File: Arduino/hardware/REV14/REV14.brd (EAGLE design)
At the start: 50 x 50 mm, 23 parts, among them IC2 ATMEGA168-AU, Q1 32768Hz, U1 RN2483, U4 SHT21, X1 SMA-142-0701-881/886, X2 SMA-142-0701-881/886

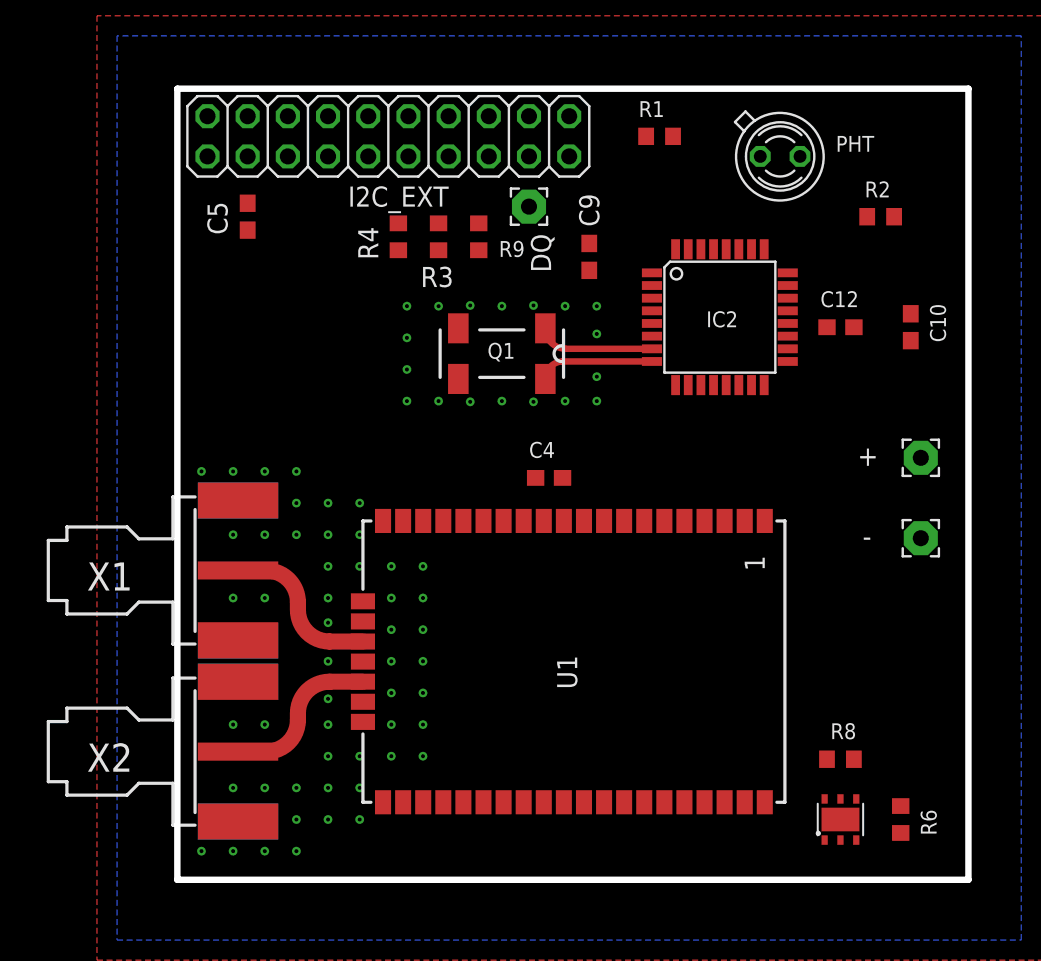
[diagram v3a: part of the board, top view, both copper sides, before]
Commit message: updated readme...
2-4 set of docs are confusing.... it makes things far more dificult for
those that do the work
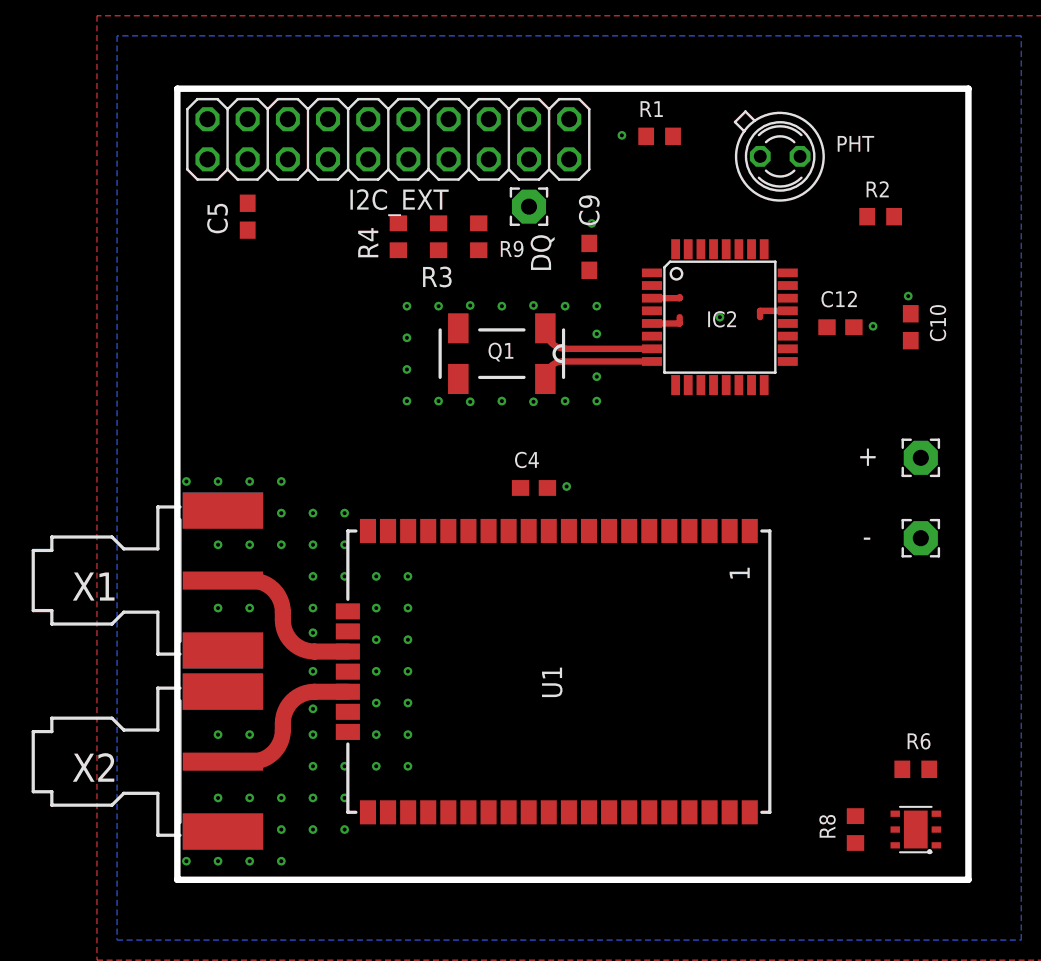
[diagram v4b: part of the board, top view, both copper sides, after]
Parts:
- moved U4 4.80 mm to (46.7, 3.17), turned to 90 degrees
- moved R8 4.55 mm to (42.9, 3.17), turned to 90 degrees
- moved R6 3.31 mm to (46.7, 6.99), turned to 0 degrees
- moved U1 1.14 mm to (37.4, 4.26)
- moved X1 1.14 mm to (0.32, 18.9)
- moved X2 1.14 mm to (0.32, 7.46)
- moved C4 1.14 mm to (22.5, 24.8)
- moved I2C_EXT 0.19 mm to (13.3, 46.8)
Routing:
- net GND: track 0.00 -> 6.13 mm, vias 69 -> 75

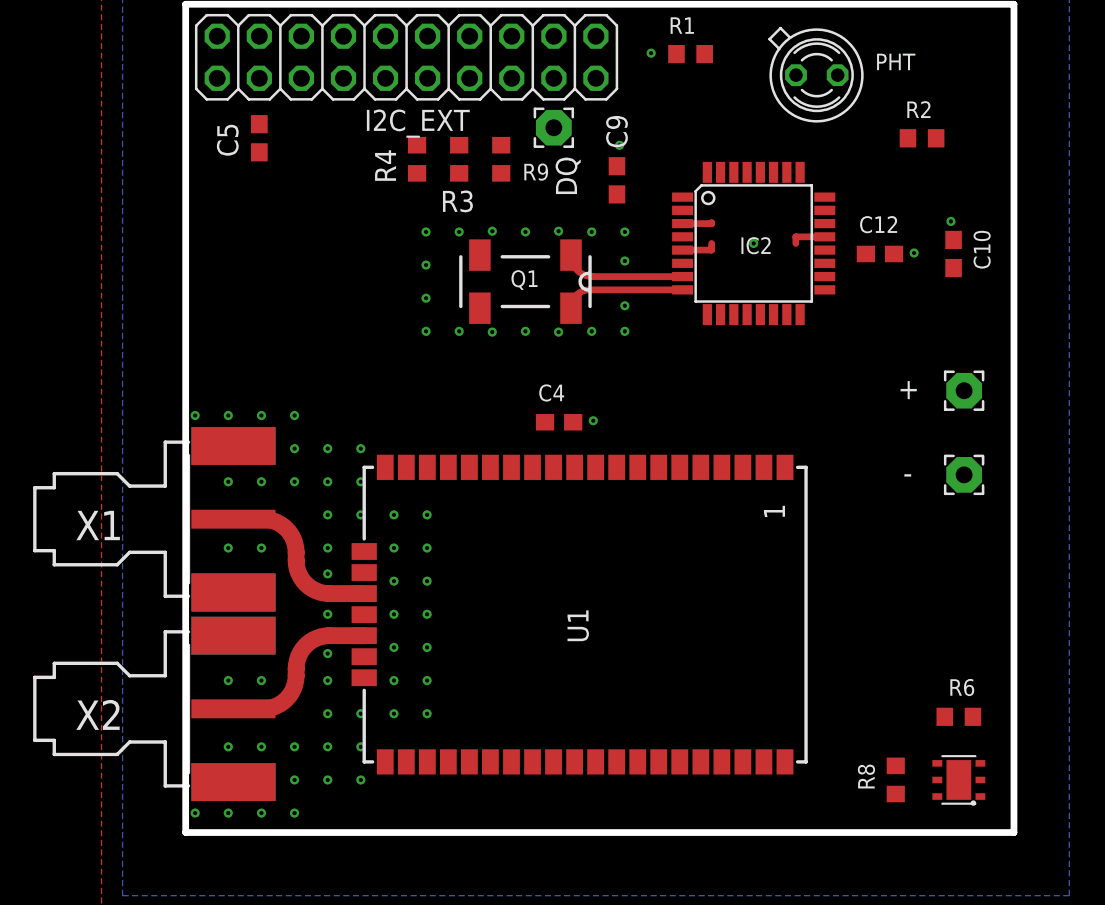
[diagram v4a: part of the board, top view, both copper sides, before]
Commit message: added ftdi for updating LoRa
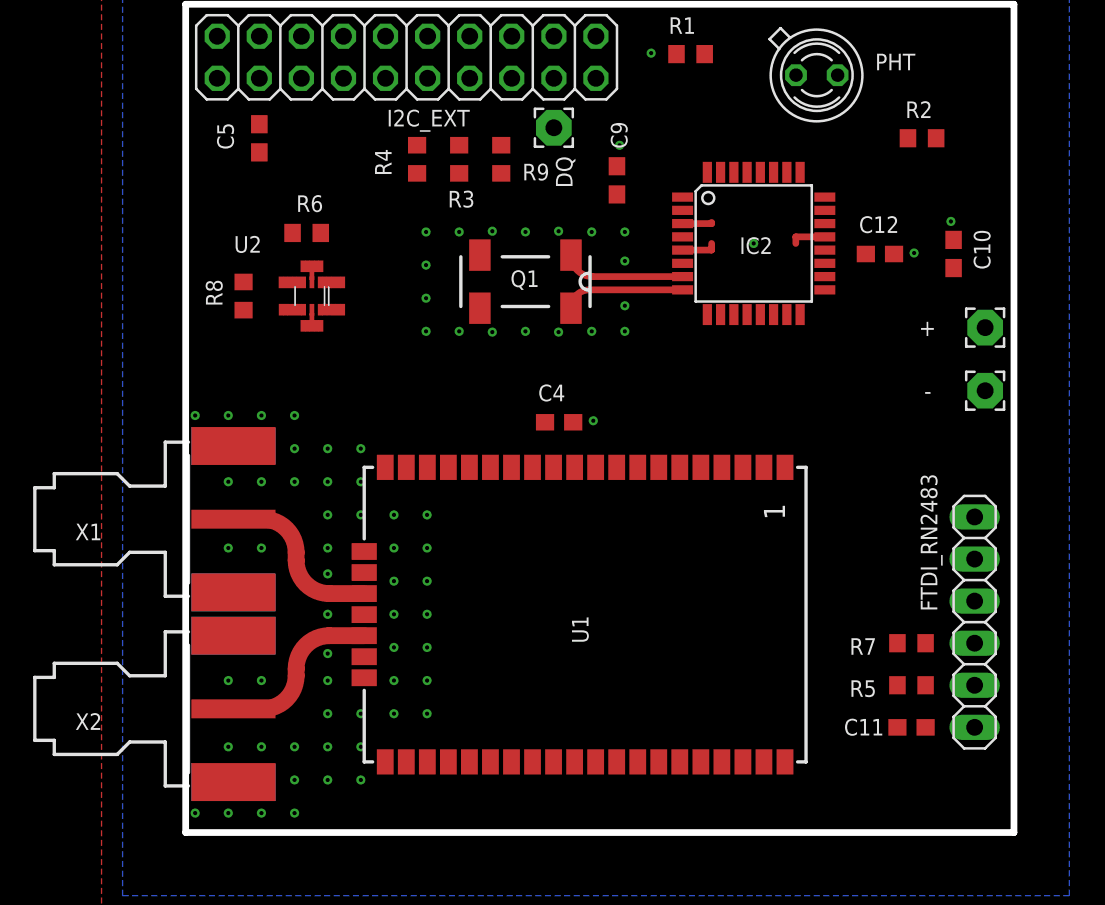
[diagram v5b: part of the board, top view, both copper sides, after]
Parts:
- removed U4: SHT21, SHT21:SHT21
- added C11: 100nF, resistor:C0603
- added FTDI_RN2483: (no value), pinhead:1X06
- added R5, R7: 10K, resistor:R0603
- added U2: TMP112, TMP112_2:TMP112
- moved R6 49.0 mm to (7.30, 36.2)
- moved R8 49.0 mm to (3.49, 32.4)
- moved - 5.24 mm to (48.3, 26.7)
- moved + 4.02 mm to (48.3, 30.5)
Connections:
- new net N$2: C11.2, FTDI_RN2483.6
- new net N$5: FTDI_RN2483.4, R7.2
- new net N$7: FTDI_RN2483.5, R5.2
- net GND: now also FTDI_RN2483.1, U2.2, U2.4; no longer U4.2, U4.P$1
- net RN2483_RESET: now also C11.1
- net RN2483_UART_CTS: now also FTDI_RN2483.2
- net RN2483_UART_RX: now also R5.1
- net RN2483_UART_TX: now also R7.1
- net SCL: now also U2.1; no longer U4.6
- net SDA: now also U2.6; no longer U4.1
- net VCC: now also FTDI_RN2483.3, U2.5; no longer U4.5

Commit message: rev 14 updated and intial routing attempt
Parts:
- moved C10 6.39 mm to (40.6, 32.1), turned to 0 degrees
- moved R8 5.71 mm to (9.21, 32.4), turned to 270 degrees
- moved U2 2.22 mm to (5.40, 32.4)
- moved R6 2.03 mm to (5.71, 37.5), turned to 180 degrees
- moved Q1 1.80 mm to (19.2, 32.0)
- moved IC2 1.80 mm to (33.0, 34.3)
- moved C9 1.80 mm to (24.8, 38.1)
- moved C12 1.42 mm to (40.6, 34.3)
- moved + 1.27 mm to (47.0, 30.5)
- moved - 1.27 mm to (47.0, 26.7)
- moved R5 1.00 mm to (42.9, 8.57)
- moved C11 1.00 mm to (42.9, 6.03)
- moved FTDI_RN2483 1.00 mm to (46.7, 12.4)
- moved R7 1.00 mm to (42.9, 11.1)
- moved DQ 0.90 mm to (22.9, 41.9)
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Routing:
- net SDA: track 0.00 -> 1.72 mm
- net SCL: track 0.00 -> 1.72 mm
- net VCC: track 0.00 -> 1.71 mm
- net GND: track 6.13 -> 6.42 mm, vias 75 -> 87

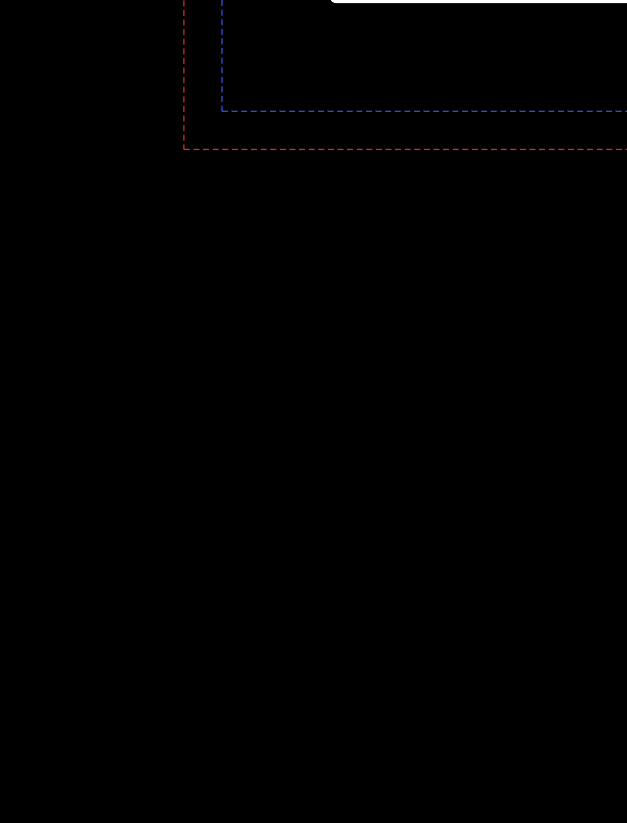
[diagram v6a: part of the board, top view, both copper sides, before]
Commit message: charge pump added
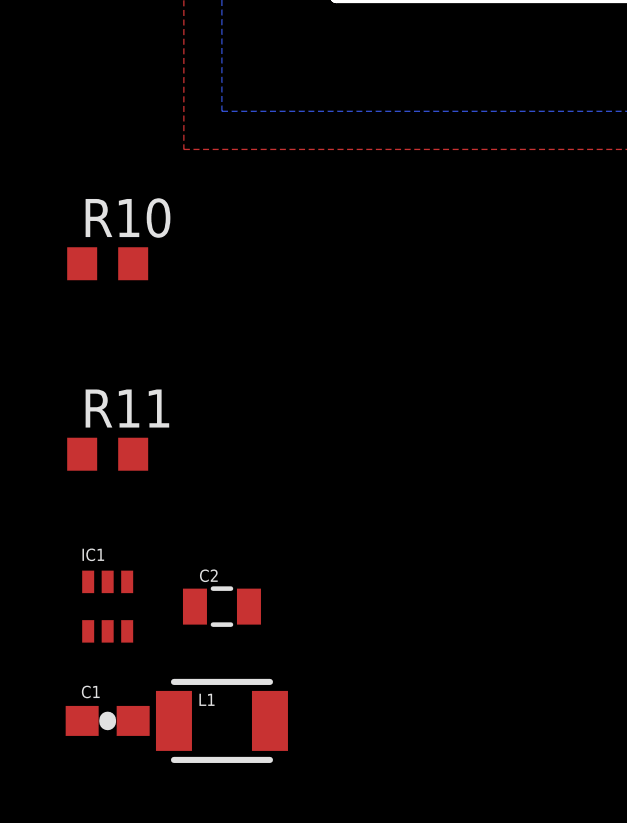
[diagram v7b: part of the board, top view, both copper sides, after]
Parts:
- added C1: 1µ, SparkFun:0603-CAP
- added C2: 10µ, SparkFun:0805
- added IC1: LTC3525, JeeLabs:SC70
- added L1: 10 µH, SparkFun:1210
- added R10, R11: 4.7K, resistor:R0603
- R5, R7: value 10K -> 4.7K
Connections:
- new net N$10: IC1.6, L1.2
- new net N$8: IC2.9, R10.2
- new net N$9: IC2.12, R11.2
- new net VCC1: C2.1, IC1.4
- net GND: now also C1.2, C2.2, IC1.2, IC1.5
- net IO_POWER_UP: now also IC2.11; no longer IC2.12
- net RN2483_RESET: now also IC2.26; no longer IC2.9
- net RN2483_UART_RTS: now also IC2.22; no longer IC2.11
- net RN2483_UART_RX: now also R10.1; no longer IC2.2
- net RN2483_UART_TX: now also R11.1; no longer IC2.1
- net VCC: now also C1.1, IC1.1, IC1.3, L1.1

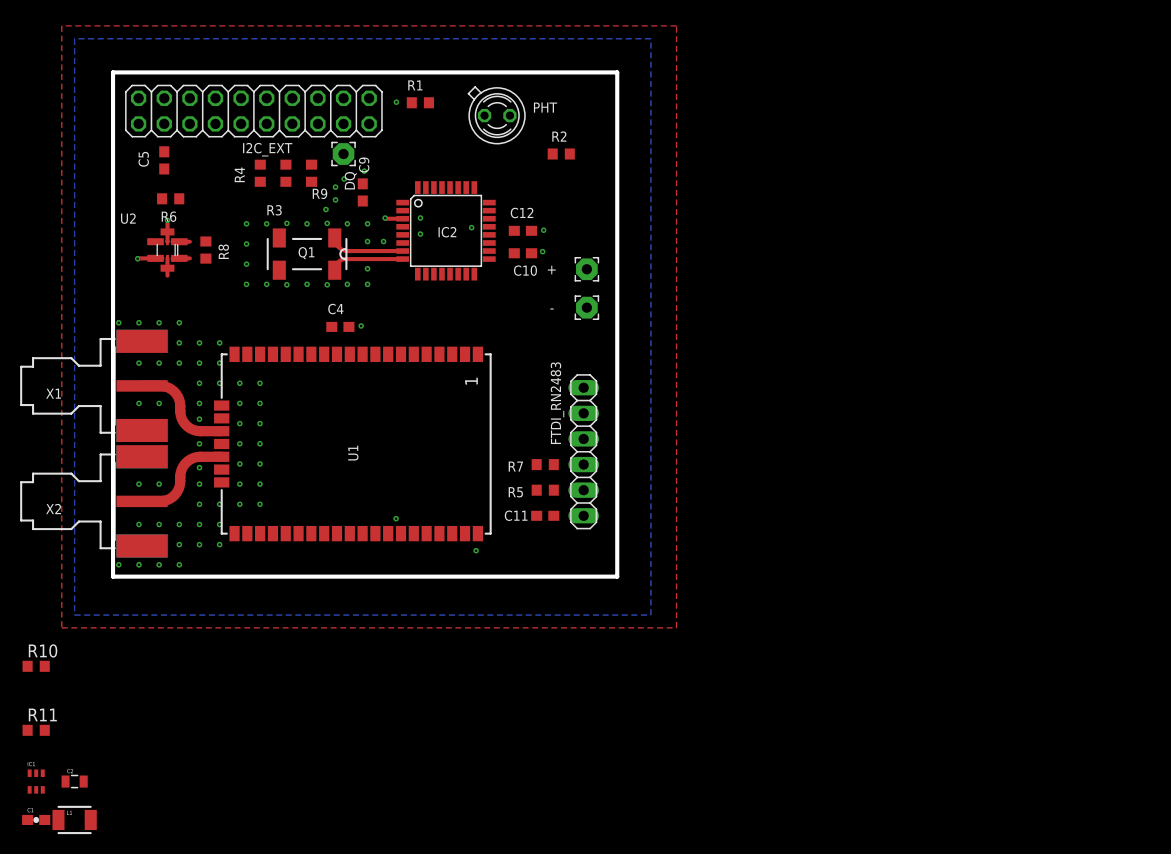
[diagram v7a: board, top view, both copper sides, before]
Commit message: routed with 1 wire left.
missing SHT21
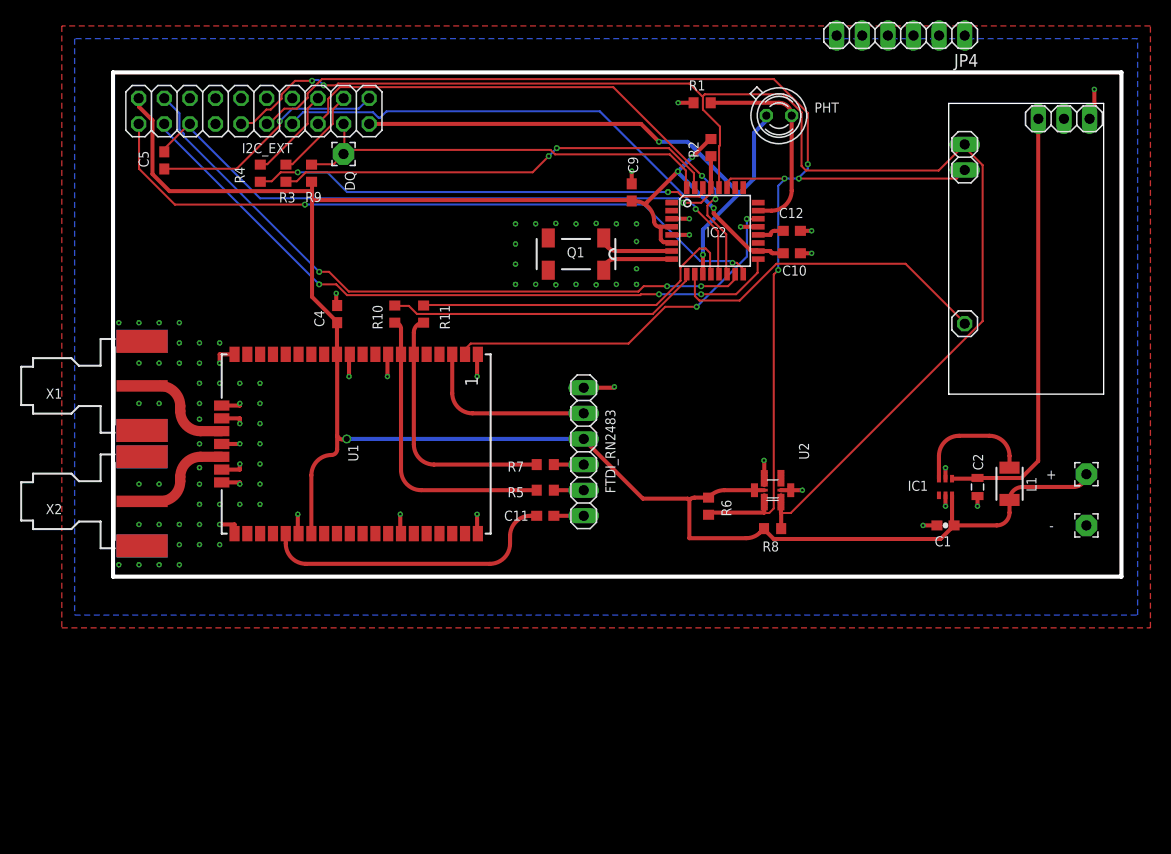
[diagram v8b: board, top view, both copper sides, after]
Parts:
- added JP1: (no value), pinhead:1X01
- added JP2: (no value), pinhead:1X02
- added JP3: (no value), pinhead:1X03
- added JP4: (no value), pinhead:1X06
- moved L1 98.5 mm to (88.9, 9.21), turned to 90 degrees
- moved C1 94.8 mm to (82.5, 5.08), turned to 180 degrees
- moved IC1 94.8 mm to (82.5, 8.89)
- moved C2 94.2 mm to (85.7, 8.89), turned to 270 degrees
- moved U2 64.6 mm to (65.4, 8.57), turned to 90 degrees
- moved R8 62.6 mm to (65.4, 4.76), turned to 180 degrees
- moved R6 61.4 mm to (59.1, 6.99), turned to 270 degrees
- moved R11 56.4 mm to (30.8, 26.0), turned to 90 degrees
- moved - 54.0 mm to (96.5, 5.08)
- moved + 53.5 mm to (96.5, 10.2)
- moved R10 49.8 mm to (27.9, 26.0), turned to 90 degrees
- moved PHT 27.9 mm to (66.0, 45.7)
- moved R1 27.9 mm to (58.4, 47.0)
- moved C10 26.7 mm to (67.3, 32.1)
- moved C12 26.7 mm to (67.3, 34.3)
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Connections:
- new net CHG_PUMP: IC1.1
- new net VOICE_NIRQ: IC2.10, JP1.1
- net GND: now also JP3.3
- net RN2483_RESET: no longer IC2.26
- net RN2483_UART_CTS: no longer IC2.10
- net SCL: now also JP2.2
- net SDA: now also JP2.1
- net VCC: no longer IC1.1
- net VCC1: now also JP3.1
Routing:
- net VCC: track 1.71 -> 220.1 mm, vias 0 -> 4
- net SCL: track 1.72 -> 141.4 mm, vias 0 -> 2
- net SDA: track 1.72 -> 130.3 mm, vias 0 -> 4
- net SPI_MISO: track 0.00 -> 69.0 mm, vias 0 -> 2
- net SPI_SCK: track 0.00 -> 68.6 mm, vias 0 -> 3
- net SPI_MOSI: track 0.00 -> 66.7 mm, vias 0 -> 3
- net RESET: track 0.00 -> 63.1 mm, vias 0 -> 1
- net IO_POWER_UP: track 0.00 -> 57.9 mm, vias 0 -> 2
- net SPI_NSS: track 0.00 -> 55.6 mm, vias 0 -> 2
- net RFM_IRQ: track 0.00 -> 52.6 mm, vias 0 -> 1
- net GND: track 6.42 -> 55.3 mm, vias 87 -> 91
- net TX: track 0.00 -> 46.0 mm, vias 0 -> 2
- net RX: track 0.00 -> 44.4 mm, vias 0 -> 2
- net D2: track 0.00 -> 43.7 mm
- net VCC1: track 0.00 -> 43.2 mm
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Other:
- board size 50 x 50 mm -> 100 x 50 mm
